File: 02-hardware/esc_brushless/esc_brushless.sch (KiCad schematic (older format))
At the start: 0 parts

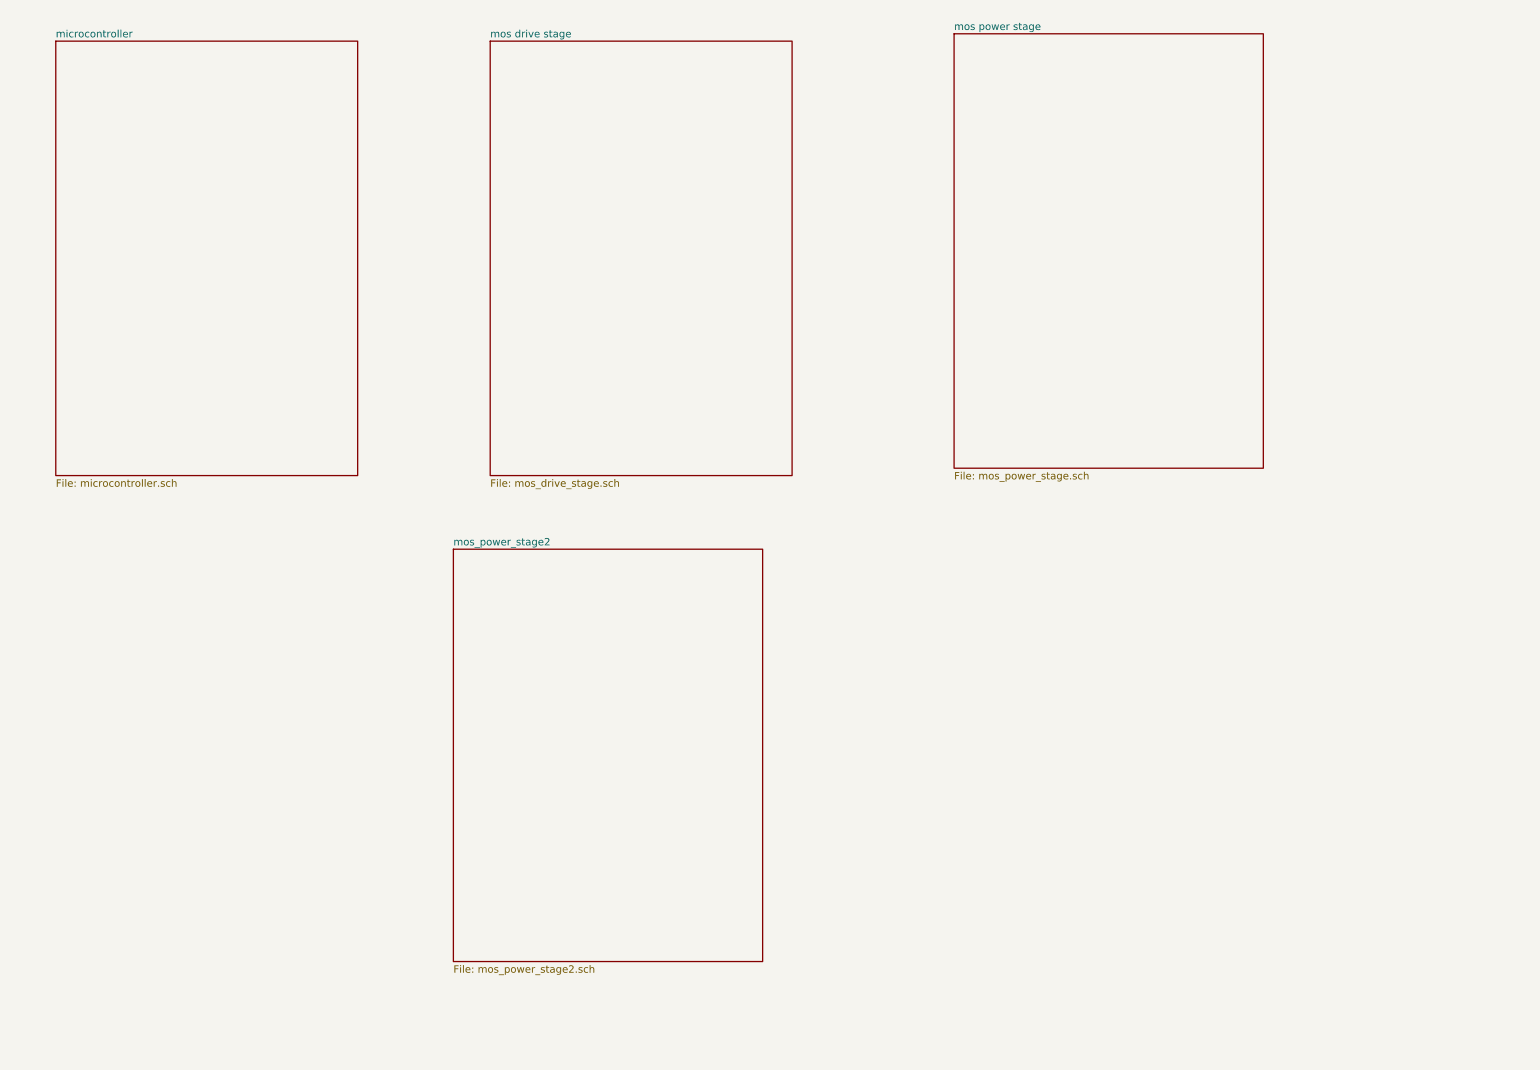
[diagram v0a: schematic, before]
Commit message: Schematics v1.0 - Architecture, MOS power stage, mos driver stage and RS485 interface
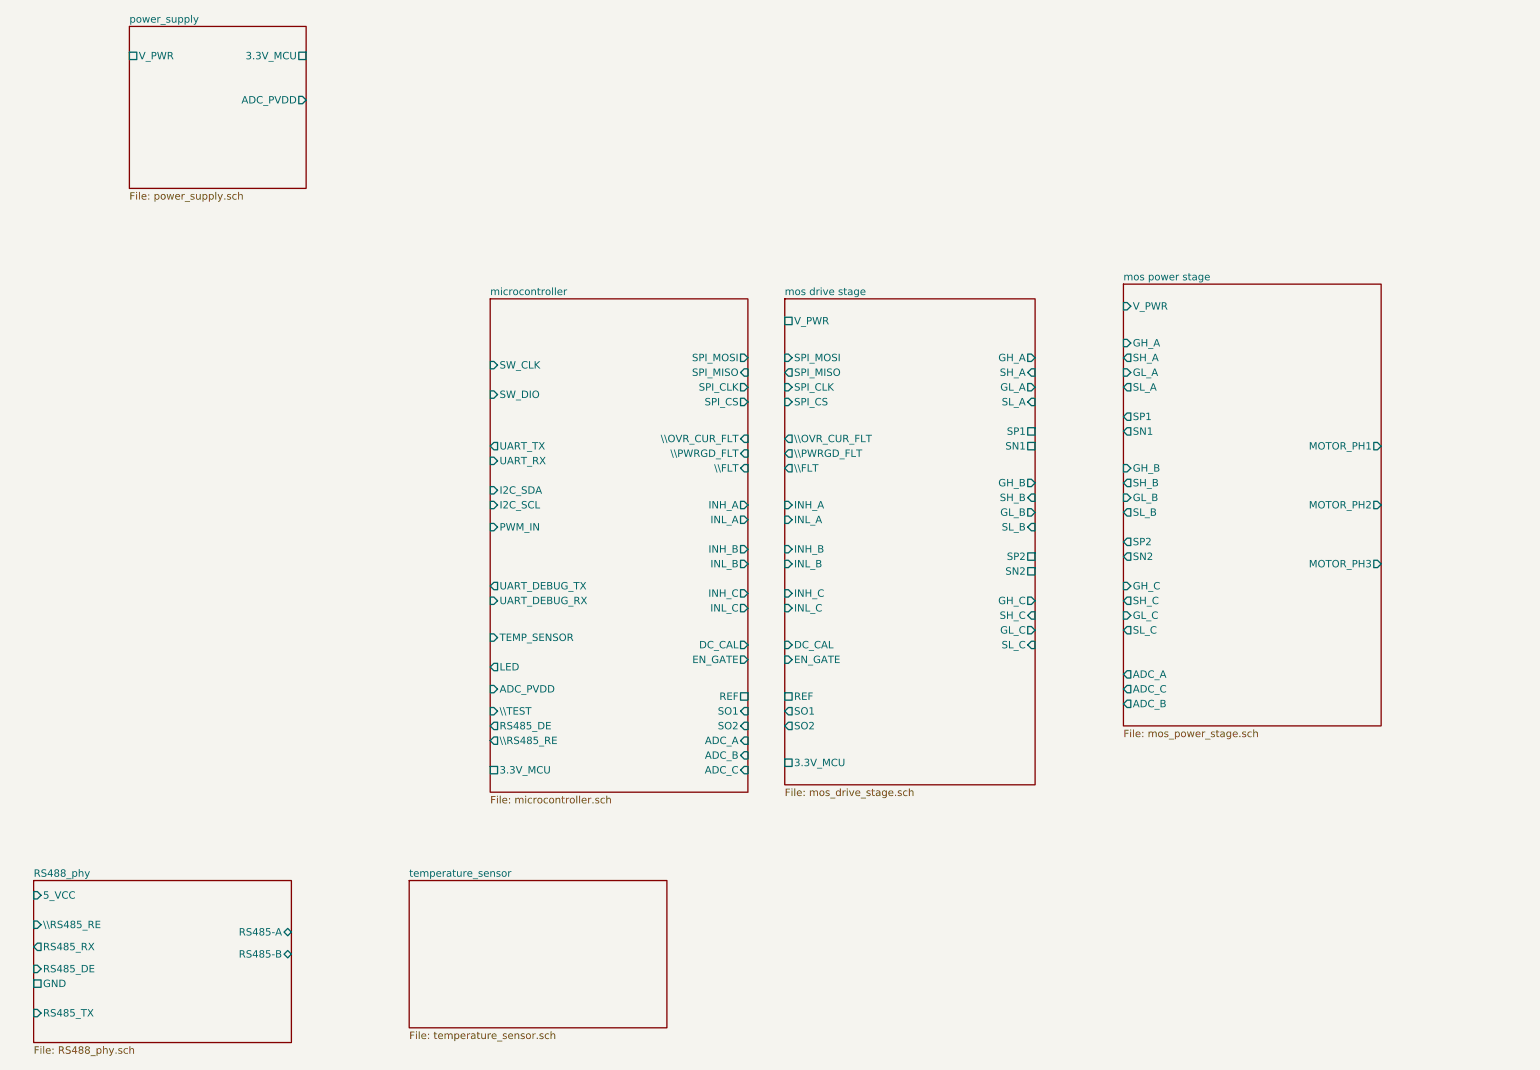
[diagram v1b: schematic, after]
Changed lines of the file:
@@
 $Descr A4 11693 8268
 encoding utf-8
-Sheet 1 5
+Sheet 1 7
 Title "ESC Brushless"
 Date "2021-02-09"
@@
 $EndDescr
 $Sheet
-S 7100 750  2100 2950
+S 8250 2450 1750 3000
 U 602453F4
 F0 "mos power stage" 50
 F1 "mos_power_stage.sch" 50
+F2 "GH_A" I L 8250 2850 50
+F3 "SH_A" O L 8250 2950 50
+F4 "GL_A" I L 8250 3050 50
+F5 "GH_B" I L 8250 3700 50
+F6 "SH_B" O L 8250 3800 50
+F7 "GL_B" I L 8250 3900 50
+F8 "GH_C" I L 8250 4500 50
+F9 "SH_C" O L 8250 4600 50
+F10 "GL_C" I L 8250 4700 50
+F11 "ADC_C" O L 8250 5200 50
+F12 "SN1" O L 8250 3450 50
+F13 "SP1" O L 8250 3350 50
+F14 "SN2" O L 8250 4300 50
+F15 "SP2" O L 8250 4200 50
+F16 "ADC_B" O L 8250 5300 50
+F17 "ADC_A" O L 8250 5100 50
+F18 "V_PWR" I L 8250 2600 50
+F19 "MOTOR_PH1" O R 10000 3550 50
+F20 "MOTOR_PH2" O R 10000 3950 50
+F21 "MOTOR_PH3" O R 10000 4350 50
+F22 "SL_C" O L 8250 4800 50
+F23 "SL_B" O L 8250 4000 50
+F24 "SL_A" O L 8250 3150 50
 $EndSheet
 $Sheet
-S 1000 800  2050 2950
+S 5950 2550 1700 3300
+U 603415C7
+F0 "mos drive stage" 50
+F1 "mos_drive_stage.sch" 50
+F2 "\\OVR_CUR_FLT" O L 5950 3500 50
+F3 "\\FLT" O L 5950 3700 50
+F4 "\\PWRGD_FLT" O L 5950 3600 50
+F5 "SPI_CS" I L 5950 3250 50
+F6 "SPI_MOSI" I L 5950 2950 50
+F7 "SPI_CLK" I L 5950 3150 50
+F8 "SPI_MISO" O L 5950 3050 50
+F9 "INH_A" I L 5950 3950 50
+F10 "INL_A" I L 5950 4050 50
+F11 "INH_B" I L 5950 4250 50
+F12 "INL_B" I L 5950 4350 50
+F13 "INH_C" I L 5950 4550 50
+F14 "INL_C" I L 5950 4650 50
+F15 "SO1" O L 5950 5350 50
+F16 "SO2" O L 5950 5450 50
+F17 "DC_CAL" I L 5950 4900 50
+F18 "SN2" U R 7650 4400 50
+F19 "SP2" U R 7650 4300 50
+F20 "SN1" U R 7650 3550 50
+F21 "SP1" U R 7650 3450 50
+F22 "EN_GATE" I L 5950 5000 50
+F23 "GL_A" O R 7650 3150 50
+F24 "SH_A" I R 7650 3050 50
+F25 "SL_A" I R 7650 3250 50
+F26 "GH_A" O R 7650 2950 50
+F27 "GL_B" O R 7650 4000 50
+F28 "SH_B" I R 7650 3900 50
+F29 "SL_B" I R 7650 4100 50
+F30 "GH_B" O R 7650 3800 50
+F31 "GL_C" O R 7650 4800 50
+F32 "SH_C" I R 7650 4700 50
+F33 "SL_C" I R 7650 4900 50
+F34 "GH_C" O R 7650 4600 50
+F35 "V_PWR" U L 5950 2700 50
+F36 "3.3V_MCU" U L 5950 5700 50
+F37 "REF" U L 5950 5250 50
+$EndSheet
+$Sheet
+S 3950 2550 1750 3350
 U 60281062
 F0 "microcontroller" 50
 F1 "microcontroller.sch" 50
+F2 "\\OVR_CUR_FLT" I R 5700 3500 50
+F3 "\\FLT" I R 5700 3700 50
+F4 "3.3V_MCU" U L 3950 5750 50
+F5 "\\PWRGD_FLT" I R 5700 3600 50
+F6 "SPI_CS" O R 5700 3250 50
+F7 "SPI_MOSI" O R 5700 2950 50
+F8 "SPI_CLK" O R 5700 3150 50
+F9 "SPI_MISO" I R 5700 3050 50
+F10 "INH_A" O R 5700 3950 50
+F11 "INL_A" O R 5700 4050 50
+F12 "INH_B" O R 5700 4250 50
+F13 "INL_B" O R 5700 4350 50
+F14 "INH_C" O R 5700 4550 50
+F15 "INL_C" O R 5700 4650 50
+F16 "SO1" I R 5700 5350 50
+F17 "SO2" I R 5700 5450 50
+F18 "DC_CAL" O R 5700 4900 50
+F19 "EN_GATE" O R 5700 5000 50
+F20 "ADC_C" I R 5700 5750 50
+F21 "ADC_B" I R 5700 5650 50
+F22 "ADC_A" I R 5700 5550 50
+F23 "UART_TX" O L 3950 3550 50
+F24 "UART_RX" I L 3950 3650 50
+F25 "I2C_SDA" I L 3950 3850 50
+F26 "I2C_SCL" I L 3950 3950 50
+F27 "PWM_IN" I L 3950 4100 50
+F28 "SW_CLK" I L 3950 3000 50
+F29 "SW_DIO" I L 3950 3200 50
+F30 "TEMP_SENSOR" I L 3950 4850 50
+F31 "ADC_PVDD" I L 3950 5200 50
+F32 "LED" O L 3950 5050 50
+F33 "\\TEST" I L 3950 5350 50
+F34 "REF" U R 5700 5250 50
+F35 "UART_DEBUG_TX" O L 3950 4500 50
+F36 "UART_DEBUG_RX" I L 3950 4600 50
+F37 "\\RS485_RE" O L 3950 5550 50
+F38 "RS485_DE" O L 3950 5450 50
 $EndSheet
 $Sheet
-S 3700 4250 2100 2800
-U 6028E64B
-F0 "mos_power_stage2" 50
-F1 "mos_power_stage2.sch" 50
+S 1500 700  1200 1100
+U 60926670
+F0 "power_supply" 50
+F1 "power_supply.sch" 50
+F2 "3.3V_MCU" U R 2700 900 50
+F3 "V_PWR" U L 1500 900 50
+F4 "ADC_PVDD" O R 2700 1200 50
 $EndSheet
 $Sheet
-S 3950 800  2050 2950
-U 603415C7
-F0 "mos drive stage" 50
-F1 "mos_drive_stage.sch" 50
+S 3400 6500 1750 1000
+U 60926813
+F0 "temperature_sensor" 50
+F1 "temperature_sensor.sch" 50
+$EndSheet
+$Sheet
+S 850  6500 1750 1100
+U 609267BC
+F0 "RS488_phy" 50
+F1 "RS488_phy.sch" 50
+F2 "5_VCC" I L 850 6600 50
+F3 "\\RS485_RE" I L 850 6800 50
+F4 "RS485_RX" O L 850 6950 50
+F5 "RS485-A" B R 2600 6850 50
+F6 "RS485-B" B R 2600 7000 50
+F7 "GND" U L 850 7200 50
+F8 "RS485_DE" I L 850 7100 50
+F9 "RS485_TX" I L 850 7400 50
 $EndSheet
 $EndSCHEMATC

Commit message: Schematics v1.0 - Architecture, microcontroler, global interconnections and IO
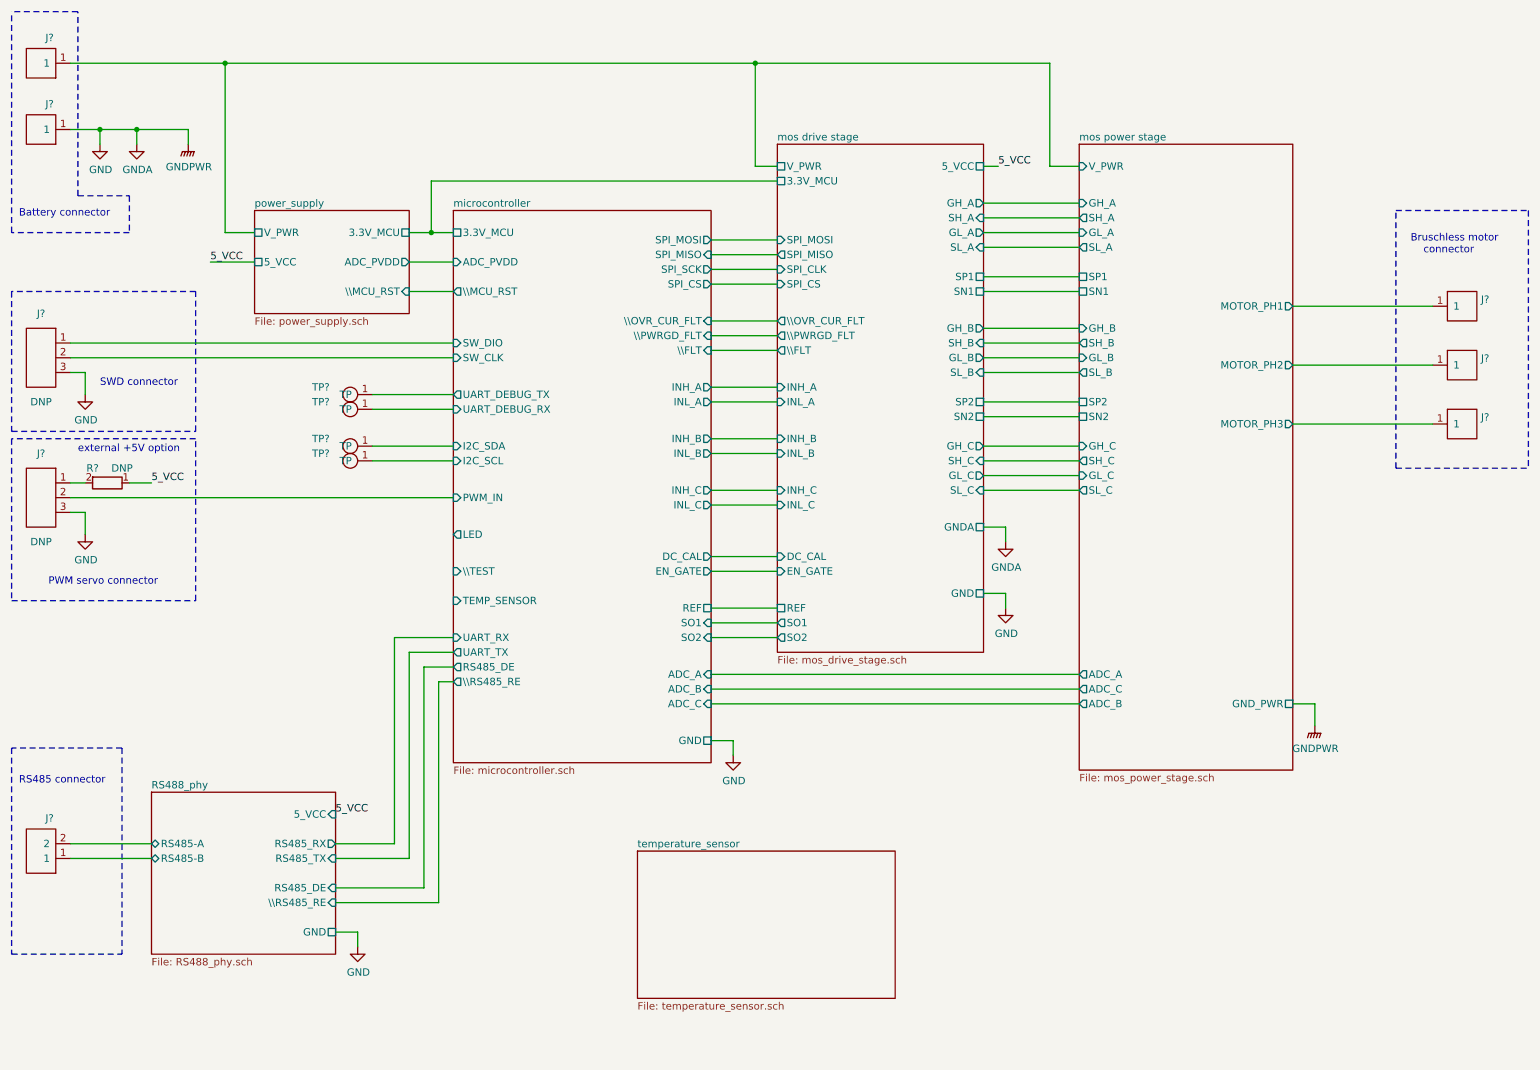
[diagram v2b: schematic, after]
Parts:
- added J? (x2): Conn_HE13_1x1_5.08V, p_Package_Misc:PinHeader_1x01_P5.08mm_Vertical, symbol p_Misc:Conn_HE13_1x1_5.08V
- added J?: Conn_HE13_1x2_2.54V, p_Package_Misc:PinHeader_1x02_P2.54mm_Vertical, symbol p_Misc:Conn_HE13_1x2_2.54V
- added J? (x2): DNP, p_Package_Misc:PinHeader_1x03_P2.54mm_Vertical, symbol esc_brushless-rescue:Conn_HE13_1x3_2.54-p_Misc
- added J? (x3): DNP, p_Package_Misc:PinHeader_1x01_P5.08mm_Vertical, symbol p_Misc:Conn_HE13_1x1_5.08V
- added R?: DNP, p_Package_Resistor_SMD:R_0603_1608Metric_Pad0.98x0.95mm_HandSolder, symbol p_Passive:R_0603
- added TP? (x4): test_point, p_Package_Misc:TP_SMD_1.25mm, symbol p_Misc:test_point
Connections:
- net RS488_phy/RS485-A: now also J?.2
- net RS488_phy/RS485-B: now also J?.1
- net microcontroller/I2C_SCL: now also TP?.1 (TP)
- net microcontroller/I2C_SDA: now also TP?.1 (TP)
- net microcontroller/PWM_IN: now also J?.2
- net microcontroller/SW_CLK: now also J?.2
- net microcontroller/SW_DIO: now also J?.1
- net microcontroller/UART_DEBUG_RX: now also TP?.1 (TP)
- net microcontroller/UART_DEBUG_TX: now also TP?.1 (TP)
- net mos drive stage/V_PWR: now also J?.1
- net mos power stage/MOTOR_PH1: now also J?.1
- net mos power stage/MOTOR_PH2: now also J?.1
- net mos power stage/MOTOR_PH3: now also J?.1
- new net: J?.1, R?.2
- new net 5_VCC: R?.1
- new net GND: J?.1, J?.3, J?.3
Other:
- note added: "Battery connector"
- note added: "Bruschless motor\n connector"
- note added: "PWM servo connector"
- note added: "RS485 connector"
- note added: "SWD connector"
- note added: "external +5V option"

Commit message: Schematics v1.0 - Architecture, LED, test
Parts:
- added D?: LED_G, p_Package_Diode_SMD:LED_0603_1608Metric, symbol p_Diode:LED_G
- added R? (x2): R_0603, p_Package_Resistor_SMD:R_0603_1608Metric_Pad0.98x0.95mm_HandSolder, symbol p_Passive:R_0603
- added R?: DNP, p_Package_Resistor_SMD:R_0603_1608Metric_Pad0.98x0.95mm_HandSolder, symbol p_Passive:R_0603
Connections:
- net GND: now also R?.2
- net microcontroller/LED: now also D?.1 (KR)
- net microcontroller/\\TEST: now also R?.1, R?.1
- new net: D?.2 (AR), R?.1
- new net 3.3V_MCU: R?.2, R?.2
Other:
- note added: "Enter test mode\n(short)"
- note added: "I2C option \nfor specific\ndesigns"
- note added: "UART debug\noption"
- note added: "if implemented"
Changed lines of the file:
@@
 $Descr A4 11693 8268
 encoding utf-8
-Sheet 1 7
+Sheet 1 6
 Title "ESC Brushless"
 Date "2021-02-09"
@@
 F5 "5_VCC" U L 2350 2300 50
 F6 "\\MCU_RST" I R 3400 2500 50
-$EndSheet
-$Sheet
-S 4950 6300 1750 1000
-U 60926813
-F0 "temperature_sensor" 50
-F1 "temperature_sensor.sch" 50
+F7 "GND" U L 2350 2500 50
 $EndSheet
 $Sheet
@@
 U 1 1 6085C419
 P 3050 3200
-F 0 "TP?" H 2800 3250 50  0000 C CNN
+F 0 "TP?" H 2800 3200 50  0000 C CNN
 F 1 "test_point" H 3037 3334 50  0001 C CNN
 F 2 "p_Package_Misc:TP_SMD_1.25mm" H 3050 3000 50  0001 C CNN
@@
 U 1 1 6085D004
 P 3050 3300
-F 0 "TP?" H 2800 3350 50  0000 C CNN
+F 0 "TP?" H 2800 3300 50  0000 C CNN
 F 1 "test_point" H 3037 3434 50  0001 C CNN
 F 2 "p_Package_Misc:TP_SMD_1.25mm" H 3050 3100 50  0001 C CNN
@@
 U 1 1 6085D0A4
 P 3050 3550
-F 0 "TP?" H 2800 3600 50  0000 C CNN
+F 0 "TP?" H 2800 3550 50  0000 C CNN
 F 1 "test_point" H 3037 3684 50  0001 C CNN
 F 2 "p_Package_Misc:TP_SMD_1.25mm" H 3050 3350 50  0001 C CNN
@@
 U 1 1 6085D196
 P 3050 3650
-F 0 "TP?" H 2800 3700 50  0000 C CNN
+F 0 "TP?" H 2800 3650 50  0000 C CNN
 F 1 "test_point" H 3037 3784 50  0001 C CNN
 F 2 "p_Package_Misc:TP_SMD_1.25mm" H 3050 3450 50  0001 C CNN
@@
 Wire Wire Line
 	3400 2500 3700 2500
+$Comp
+L p_Diode:LED_G D?
+U 1 1 60B76269
+P 3100 4150
+F 0 "D?" H 3100 4300 50  0000 C CNN
+F 1 "LED_G" H 3100 4050 50  0000 C CNN
+F 2 "p_Package_Diode_SMD:LED_0603_1608Metric" H 3200 4050 50  0001 C CNN
+F 3 "" H 3200 4050 50  0001 C CNN
+	1    3100 4150
+	1    0    0    -1
+$EndComp
+$Comp
+L p_Passive:R_0603 R?
+U 1 1 60B78CC7
+P 2600 4150
+F 0 "R?" V 2500 4050 50  0000 C CNN
+F 1 "R_0603" V 2500 4300 50  0000 C CNN
+F 2 "p_Package_Resistor_SMD:R_0603_1608Metric_Pad0.98x0.95mm_HandSolder" H 2600 4150 50  0001 C CNN
+F 3 "" H 2600 4150 50  0001 C CNN
+	1    2600 4150
+	0    1    1    0
+$EndComp
+Wire Wire Line
+	2750 4150 2850 4150
+Wire Wire Line
+	2450 4150 2050 4150
+Text Label 2050 4150 0    50   ~ 0
+3.3V_MCU
+Text Label 3550 1750 0    50   ~ 0
+3.3V_MCU
+$Comp
+L p_Passive:R_0603 R?
+U 1 1 60B8810F
+P 2600 4400
+F 0 "R?" V 2500 4300 50  0000 C CNN
+F 1 "R_0603" V 2500 4550 50  0000 C CNN
+F 2 "p_Package_Resistor_SMD:R_0603_1608Metric_Pad0.98x0.95mm_HandSolder" H 2600 4400 50  0001 C CNN
+F 3 "" H 2600 4400 50  0001 C CNN
+	1    2600 4400
+	0    1    1    0
+$EndComp
+Wire Wire Line
+	2450 4400 2050 4400
+Text Label 2050 4400 0    50   ~ 0
+3.3V_MCU
+$Comp
+L p_Passive:R_0603 R?
+U 1 1 60B93F2C
+P 2600 4700
+F 0 "R?" V 2500 4600 50  0000 C CNN
+F 1 "DNP" V 2500 4800 50  0000 C CNN
+F 2 "p_Package_Resistor_SMD:R_0603_1608Metric_Pad0.98x0.95mm_HandSolder" H 2600 4700 50  0001 C CNN
+F 3 "" H 2600 4700 50  0001 C CNN
+	1    2600 4700
+	0    1    1    0
+$EndComp
+Wire Wire Line
+	2750 4700 2800 4700
+$Comp
+L power:GND #PWR?
+U 1 1 60B9925A
+P 2350 4750
+F 0 "#PWR?" H 2350 4500 50  0001 C CNN
+F 1 "GND" H 2355 4577 50  0000 C CNN
+F 2 "" H 2350 4750 50  0001 C CNN
+F 3 "" H 2350 4750 50  0001 C CNN
+	1    2350 4750
+	1    0    0    -1
+$EndComp
+Wire Wire Line
+	2450 4700 2350 4700
+Wire Wire Line
+	2350 4700 2350 4750
+Wire Wire Line
+	2800 4700 2800 4400
+Wire Wire Line
+	3350 4150 3700 4150
+Wire Wire Line
+	2750 4400 2800 4400
+Connection ~ 2800 4400
+Wire Wire Line
+	2800 4400 3700 4400
+Wire Notes Line width 12
+	2850 5250 2850 4500
+Text Notes 2100 5100 0    50   ~ 0
+Enter test mode\n(short)
+Wire Notes Line width 12
+	2050 4500 2050 5250
+Text Notes 2100 5200 0    50   ~ 0
+if implemented
+Wire Notes Line width 12
+	2050 5250 2850 5250
+Wire Notes Line width 12
+	2050 4500 2850 4500
+$Comp
+L power:GND #PWR?
+U 1 1 60BEFFEA
+P 2200 2600
+F 0 "#PWR?" H 2200 2350 50  0001 C CNN
+F 1 "GND" H 2205 2427 50  0000 C CNN
+F 2 "" H 2200 2600 50  0001 C CNN
+F 3 "" H 2200 2600 50  0001 C CNN
+	1    2200 2600
+	1    0    0    -1
+$EndComp
+Wire Wire Line
+	2350 2500 2200 2500
+Wire Wire Line
+	2200 2500 2200 2600
+Wire Notes Line width 12
+	3200 3400 2150 3400
+Text Notes 2200 3300 0    50   ~ 0
+UART debug\noption
+Wire Notes Line width 12
+	3200 3450 2150 3450
+Wire Notes Line width 12
+	2150 3450 2150 3750
+Wire Notes Line width 12
+	2150 3750 3200 3750
+Wire Notes Line width 12
+	3200 3750 3200 3450
+Wire Notes Line width 12
+	3200 3400 3200 3100
+Wire Notes Line width 12
+	3200 3100 2150 3100
+Wire Notes Line width 12
+	2150 3100 2150 3400
+Text Notes 2200 3700 0    50   ~ 0
+I2C option \nfor specific\ndesigns
 $EndSCHEMATC
